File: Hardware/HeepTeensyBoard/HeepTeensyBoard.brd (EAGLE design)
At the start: 100 x 80 mm, 29 parts, among them J1 MAGJACK, Q1 25MHz, U1 ENC28J60-SO

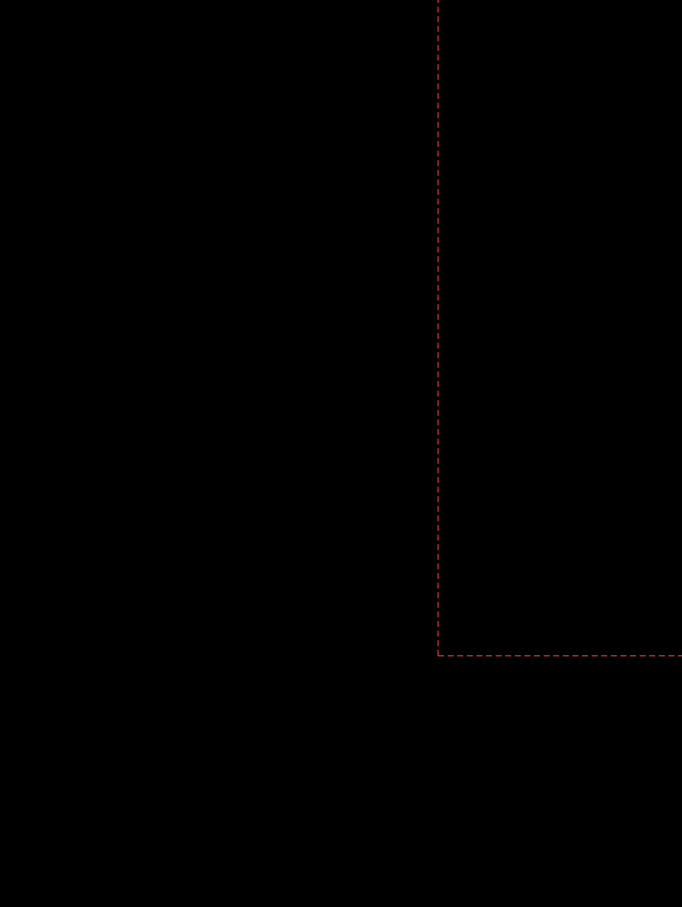
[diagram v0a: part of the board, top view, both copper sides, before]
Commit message: Added power inputs
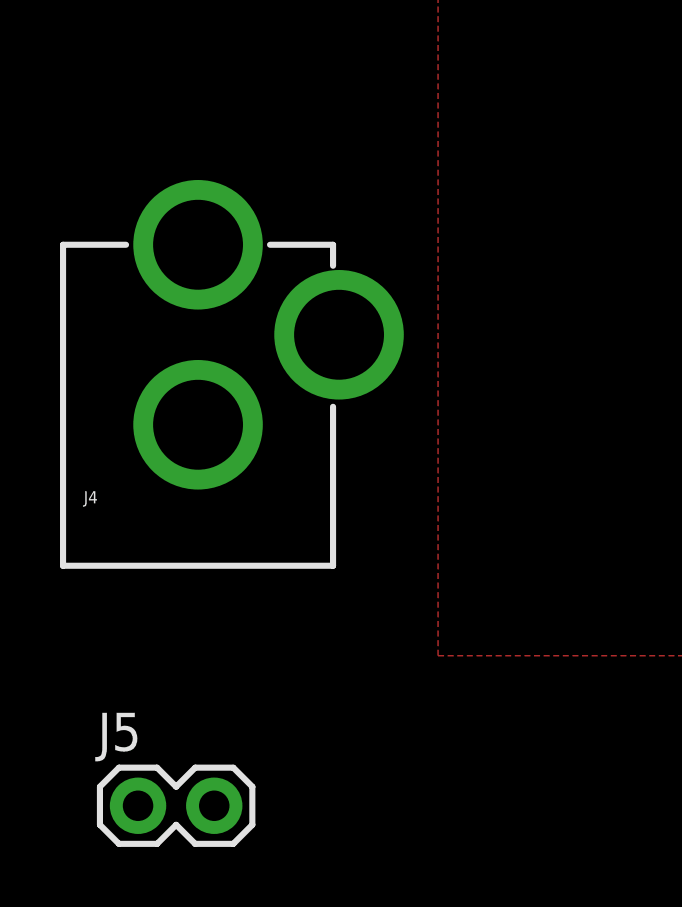
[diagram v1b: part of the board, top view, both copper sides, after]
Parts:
- added J4: POWER_JACKPTH, SparkFun-Connectors:POWER_JACK_PTH
- added J5: (no value), SparkFun-Connectors:1X02
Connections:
- net GND: now also J4.GND, J4.GNDBREAK, J5.1
- net VIN: now also J4.PWR, J5.2
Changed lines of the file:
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@@
 </element>
 <element name="R10" library="SparkFun-Passives" package="0603-RES" value="200" x="8.7" y="42.15"/>
+<element name="J4" library="SparkFun-Connectors" package="POWER_JACK_PTH" value="POWER_JACKPTH" x="-25" y="-5">
+<attribute name="PROD_ID" value="CONN-08197" x="-25" y="-5" size="1.778" layer="27" display="off"/>
+</element>
+<element name="J5" library="SparkFun-Connectors" package="1X02" value="" x="-27" y="-10"/>
 </elements>
 <signals>
@@
 <vertex x="-17" y="86"/>
 </polygon>
+<contactref element="J4" pad="GNDBREAK"/>
+<contactref element="J4" pad="GND"/>
+<contactref element="J5" pad="1"/>
+<wire x1="-25" y1="2.7" x2="-27" y2="-10" width="0" layer="19" extent="1-1"/>
+<wire x1="-20.3" y1="5.7" x2="-25" y2="2.7" width="0" layer="19" extent="1-1"/>
+<wire x1="2.54" y1="6.35" x2="-20.3" y2="5.7" width="0" layer="19" extent="1-1"/>
 </signal>
 <signal name="LEDA">
@@
 <contactref element="U$1" pad="VIN"/>
 <contactref element="J3" pad="1"/>
-<wire x1="2.54" y1="3.81" x2="6.35" y2="3.81" width="0" layer="19" extent="1-1"/>
+<contactref element="J4" pad="PWR"/>
+<contactref element="J5" pad="2"/>
+<wire x1="-25" y1="8.7" x2="-24.46" y2="-10" width="0" layer="19" extent="1-1"/>
+<wire x1="2.54" y1="3.81" x2="-25" y2="8.7" width="0" layer="19" extent="1-1"/>
+<wire x1="6.35" y1="3.81" x2="2.54" y2="3.81" width="0" layer="19" extent="1-1"/>
 </signal>
 <signal name="TEENSY14">

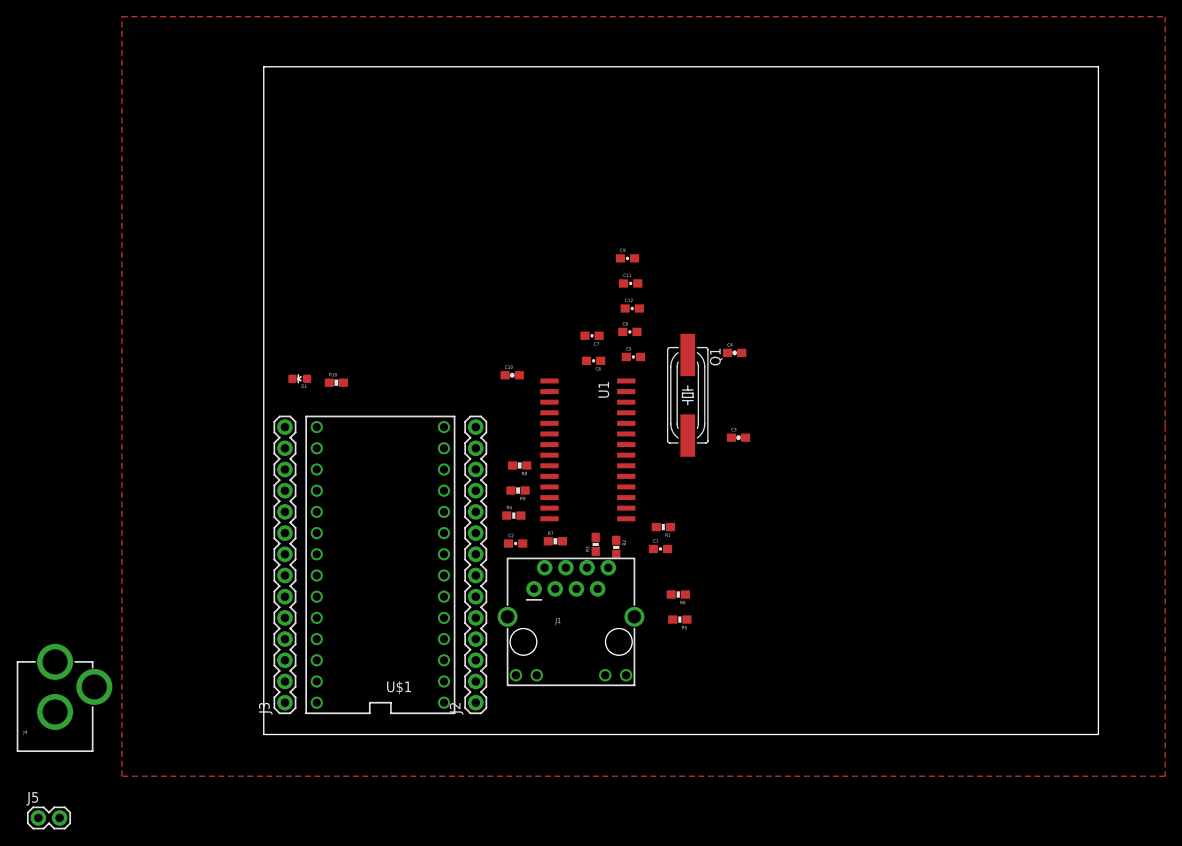
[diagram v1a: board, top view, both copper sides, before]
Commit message: #151 Rearranged capacitors more intelligently
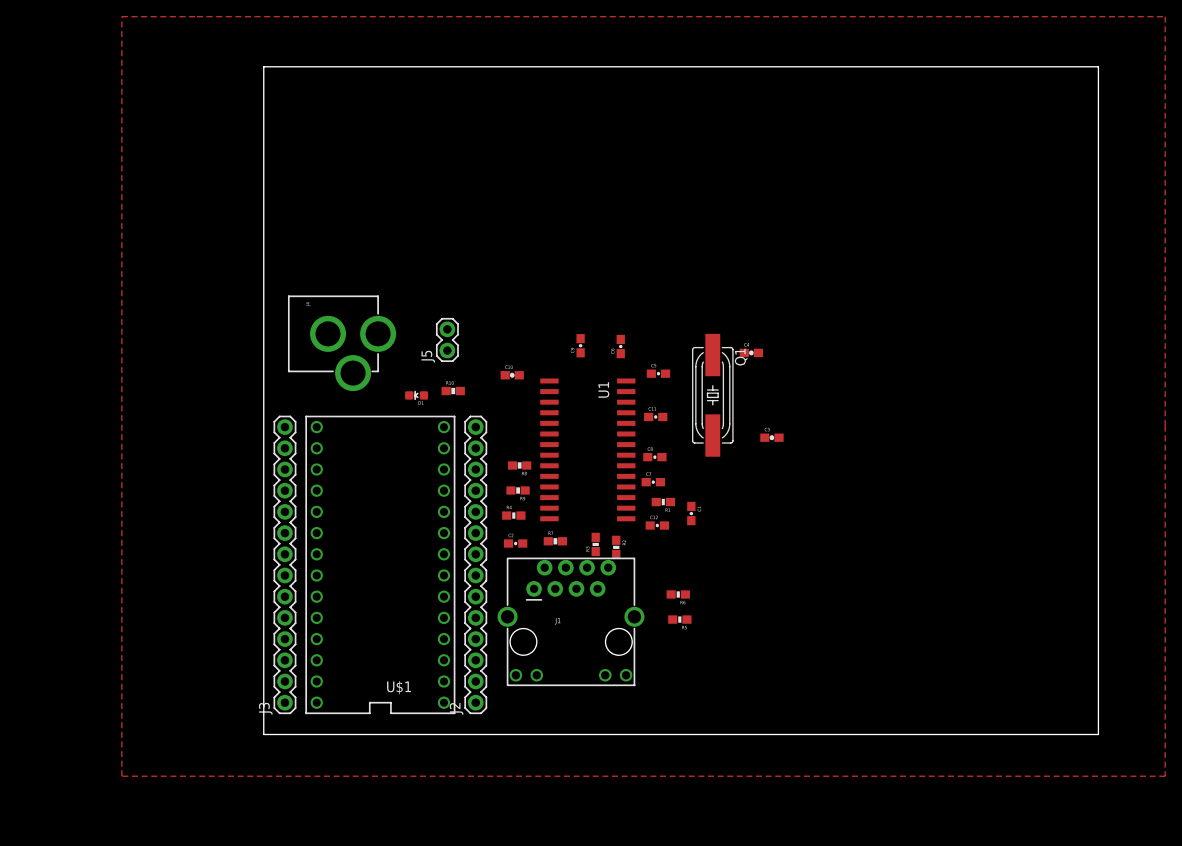
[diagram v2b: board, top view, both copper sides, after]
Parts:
- moved J5 74.4 mm to (22.0, 46.0), turned to 90 degrees
- moved J4 58.6 mm to (0.00, 48.0), turned to 270 degrees
- moved C12 26.2 mm to (47.1, 25.0)
- moved C7 19.0 mm to (46.7, 30.2), turned to 0 degrees
- moved C11 16.3 mm to (47.0, 38.0)
- moved C8 15.3 mm to (46.9, 33.2)
- moved D1 14.1 mm to (18.3, 40.6)
- moved R10 14.0 mm to (22.7, 41.1)
- moved C9 11.9 mm to (38.0, 46.6), turned to 90 degrees
- moved C1 5.63 mm to (51.2, 26.5), turned to 270 degrees
- moved C3 4.00 mm to (60.9, 35.6)
- moved C6 3.67 mm to (42.8, 46.5), turned to 90 degrees
- moved C5 3.61 mm to (47.3, 43.2)
- moved Q1 3.00 mm to (53.8, 40.6)
- moved R1 3.00 mm to (47.9, 27.9)
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
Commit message: #151 Begin Tracerouting
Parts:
- moved R3 10.1 mm to (30.6, 26.8), turned to 0 degrees
- moved R2 7.72 mm to (47.1, 28.4), turned to 0 degrees
- moved R5 6.35 mm to (47.0, 19.5)
- moved C3 5.39 mm to (58.1, 31.0)
- moved C4 5.20 mm to (58.5, 40.5)
- moved C2 5.14 mm to (28.0, 27.5), turned to 270 degrees
- moved Q1 5.00 mm to (52.8, 35.7)
- moved R6 4.94 mm to (47.1, 21.0)
- moved C9 2.83 mm to (40.8, 46.2)
- moved R4 2.18 mm to (30.6, 28.3)
- moved D1 1.26 mm to (17.9, 41.8)
- moved R10 1.22 mm to (21.7, 41.9)
- moved R1 1.20 mm to (47.1, 26.9)
- moved C8 1.00 mm to (47.0, 32.2)
- moved R9 1.00 mm to (30.6, 30.2)
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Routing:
- net N$2: track 0.00 -> 16.1 mm
- net N$1: track 0.00 -> 12.9 mm

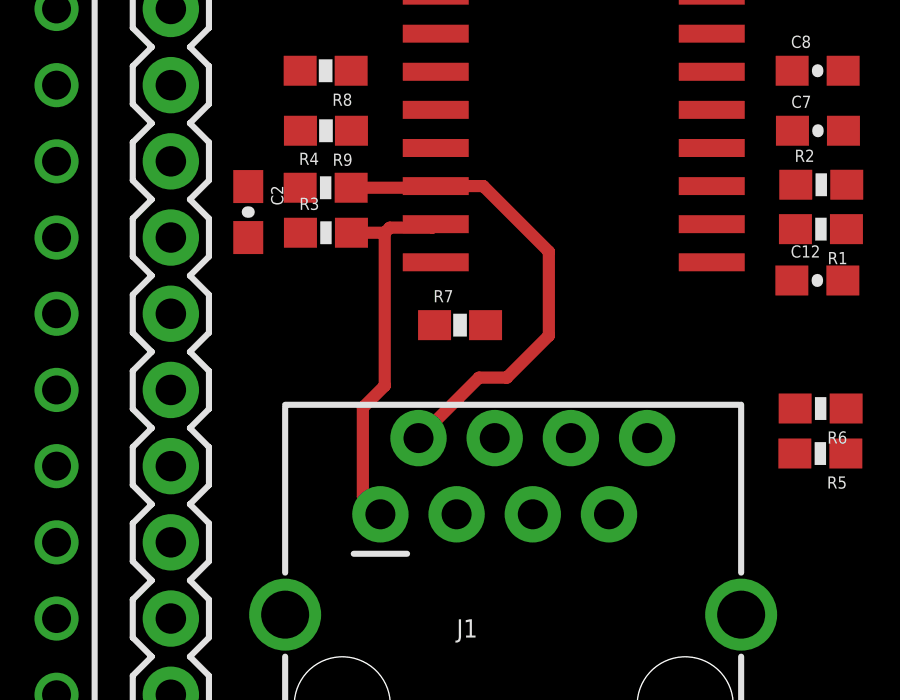
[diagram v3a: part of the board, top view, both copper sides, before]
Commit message: #151 Initial organization of components on board
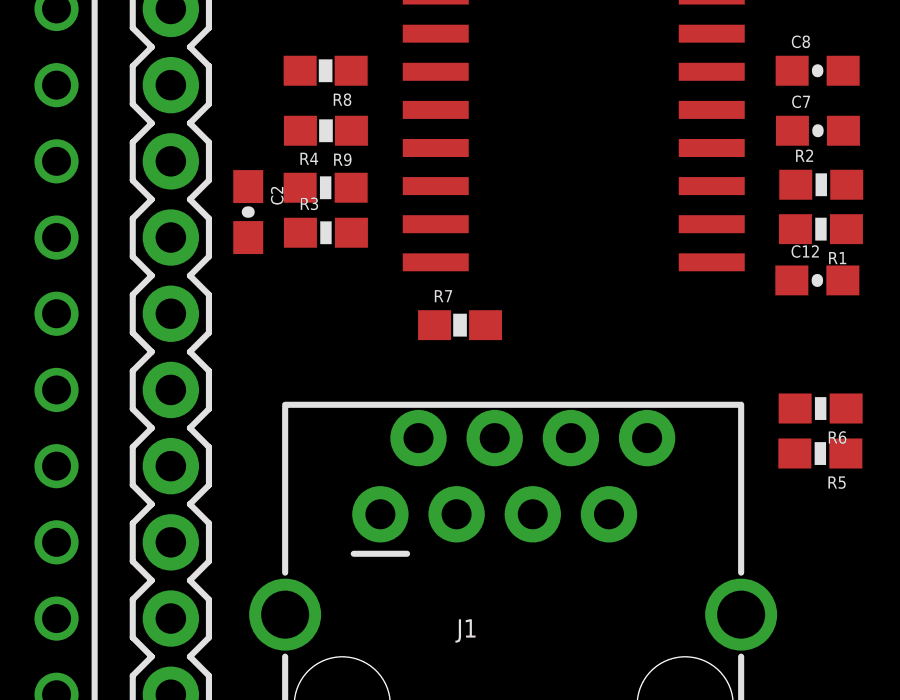
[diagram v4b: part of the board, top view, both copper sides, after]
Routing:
- net N$2: track 16.1 -> 0.00 mm
- net N$1: track 12.9 -> 0.00 mm
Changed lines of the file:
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@@
 <contactref element="J1" pad="1"/>
 <contactref element="R3" pad="2"/>
-<wire x1="31.42" y1="26.83" x2="32.53" y2="26.83" width="0.4064" layer="1"/>
-<wire x1="32.53" y1="26.83" x2="32.7" y2="27" width="0.4064" layer="1"/>
-<wire x1="32.7" y1="27" x2="34.115" y2="27" width="0.4064" layer="1"/>
-<wire x1="34.115" y1="27" x2="34.23" y2="27.115" width="0.4064" layer="1"/>
-<wire x1="32.53" y1="26.83" x2="32.53" y2="21.73" width="0.4064" layer="1"/>
-<wire x1="32.53" y1="21.73" x2="31.8" y2="21" width="0.4064" layer="1"/>
-<wire x1="31.8" y1="21" x2="31.8" y2="18.03" width="0.4064" layer="1"/>
-<wire x1="31.8" y1="18.03" x2="32.385" y2="17.445" width="0.4064" layer="1"/>
+<wire x1="31.42" y1="26.83" x2="34.23" y2="27.115" width="0" layer="19" extent="1-1"/>
+<wire x1="32.385" y1="17.445" x2="31.42" y2="26.83" width="0" layer="19" extent="1-1"/>
 </signal>
 <signal name="N$2">
@@
 <contactref element="J1" pad="2"/>
 <contactref element="R4" pad="2"/>
-<wire x1="31.41" y1="28.33" x2="34.23" y2="28.33" width="0.4064" layer="1"/>
-<wire x1="34.23" y1="28.33" x2="34.23" y2="28.385" width="0.4064" layer="1"/>
-<wire x1="34.23" y1="28.385" x2="35.815" y2="28.385" width="0.4064" layer="1"/>
-<wire x1="35.815" y1="28.385" x2="38" y2="26.2" width="0.4064" layer="1"/>
-<wire x1="38" y1="26.2" x2="38" y2="23.4" width="0.4064" layer="1"/>
-<wire x1="38" y1="23.4" x2="36.6" y2="22" width="0.4064" layer="1"/>
-<wire x1="36.6" y1="22" x2="35.67" y2="22" width="0.4064" layer="1"/>
-<wire x1="35.67" y1="22" x2="33.655" y2="19.985" width="0.4064" layer="1"/>
+<wire x1="31.41" y1="28.33" x2="34.23" y2="28.385" width="0" layer="19" extent="1-1"/>
+<wire x1="33.655" y1="19.985" x2="34.23" y2="28.385" width="0" layer="19" extent="1-1"/>
 </signal>
 <signal name="N$3">
@@
 <contactref element="J4" pad="GND"/>
 <contactref element="J5" pad="1"/>
-<wire x1="35.89" y1="23.75" x2="34.23" y2="29.655" width="0" layer="19" extent="1-1"/>
 </signal>
 <signal name="LEDA">

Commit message: #151 First full board layout
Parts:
- moved R5 1.30 mm to (47.0, 18.2)
- moved R7 1.20 mm to (33.8, 23.8)
- moved R2 0.06 mm to (47.1, 28.5), turned to 180 degrees
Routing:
- net 3.3V: track 0.00 -> 141.3 mm, vias 0 -> 4
- net VIN: track 0.00 -> 62.2 mm, vias 0 -> 1
- net #RESET: track 0.00 -> 41.1 mm, vias 0 -> 1
- net LEDB: track 0.00 -> 40.5 mm, vias 0 -> 1
- net LEDA: track 0.00 -> 40.3 mm
- net SCK: track 0.00 -> 34.0 mm
- net N$7: track 0.00 -> 21.1 mm, vias 0 -> 2
- net N$6: track 0.00 -> 19.7 mm, vias 0 -> 1
- net N$4: track 0.00 -> 16.1 mm
- net N$12: track 0.00 -> 15.9 mm
- net N$13: track 0.00 -> 15.6 mm
- net N$2: track 0.00 -> 14.6 mm
- net #CS: track 0.00 -> 14.2 mm
- net SO: track 0.00 -> 13.0 mm
- net N$10: track 0.00 -> 12.9 mm
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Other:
- board size 100 x 80 mm -> 61 x 54 mm
